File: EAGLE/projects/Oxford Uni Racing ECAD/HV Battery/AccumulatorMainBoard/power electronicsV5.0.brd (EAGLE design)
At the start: 167.6 x 103.8 mm, 82 parts, among them IC1 4043D, IC2 SE555D, IC9 4011D, K2 T9AS5D12-12=T9A, K6 T9AS1D12-48=T9A, K7 T9AS1D12-48=T9A, Q1 BSS138, Q2 BSS138, Q3 BSS138, Q4 BSS138

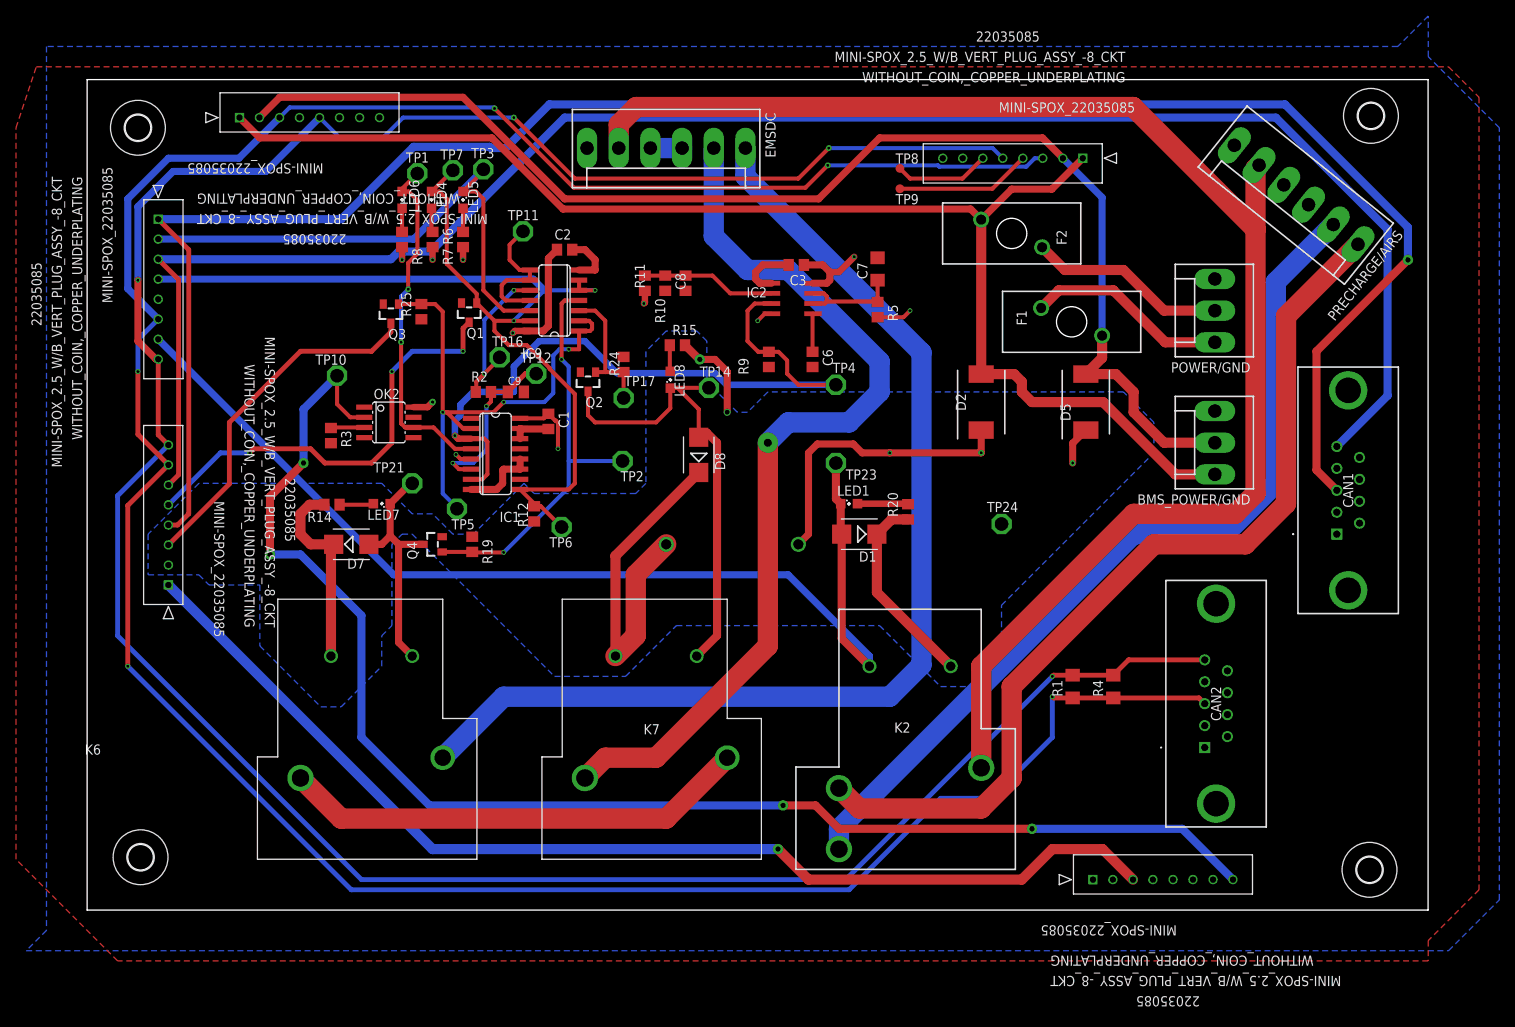
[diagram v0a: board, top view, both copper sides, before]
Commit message: Mainboard v5.1
Fixes the +12V  connections
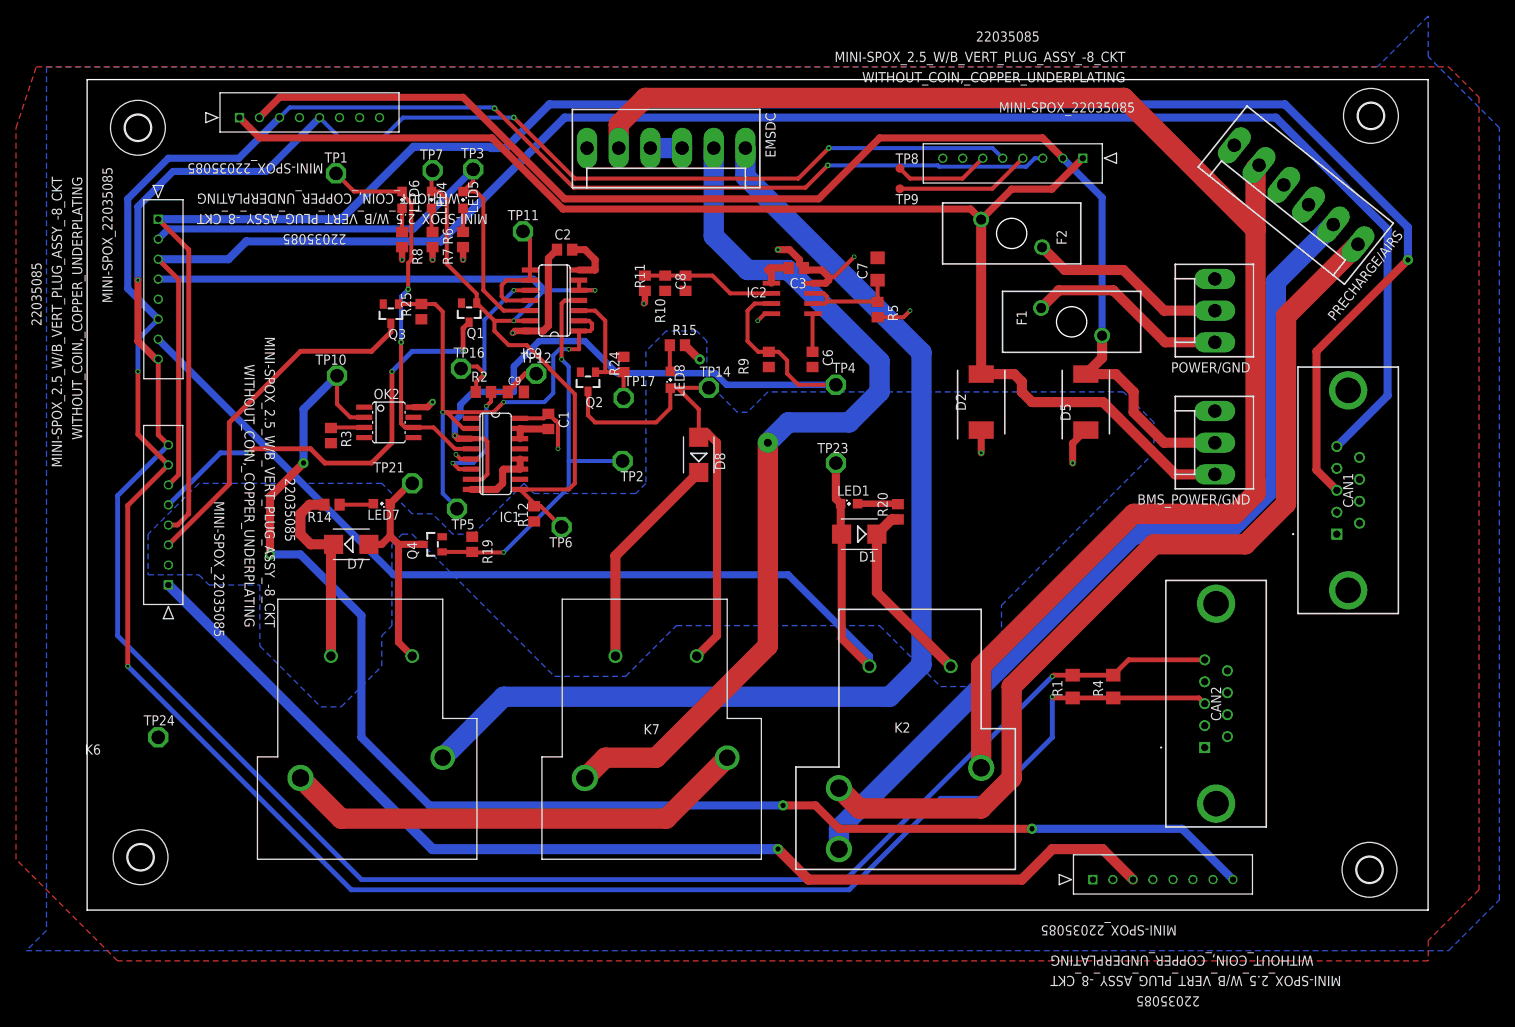
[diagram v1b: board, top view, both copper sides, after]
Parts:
- moved TP24 108.7 mm to (8.89, 21.6)
- moved TP1 10.2 mm to (31.1, 92.1)
- moved TP16 5.02 mm to (46.7, 67.7)
- moved TP7 2.54 mm to (43.2, 92.5)
- moved TP3 1.27 mm to (48.3, 92.6)
- moved R20 1.27 mm to (101.3, 49.8)
- moved C3 0.38 mm to (88.6, 80.3)
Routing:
- net +12V: track 147.5 -> 86.0 mm, vias 7 -> 3
- net N$5: track 44.2 -> 49.2 mm
- net +3V3: track 52.6 -> 56.7 mm, vias 11 -> 12
- net GND: track 28.5 -> 25.5 mm
- net N$6: track 17.5 -> 15.4 mm
- net CHARGE_SAFE: track 69.3 -> 67.5 mm
- net N$22: track 6.34 -> 5.07 mm
- net DISCHARGE_ENABLE: track 132.3 -> 131.2 mm
- net N$11: track 187.0 -> 187.9 mm
- net N$1: track 19.5 -> 20.1 mm
